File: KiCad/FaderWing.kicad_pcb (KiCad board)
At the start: 2 copper layers, 108 x 240 mm, 242 parts, among them J1 USB_C_Receptacle_USB2.0, SW1 Encoder_Switch, SW10 SW_Push, SW11 Encoder_Switch, SW12 SW_Push, SW13 SW_Push, SW14 SW_Push, SW15 SW_Push, SW16 Encoder_Switch, SW17 SW_Push, SW18 SW_Push, SW19 SW_Push, SW2 SW_Push, SW20 SW_Push, SW21 Encoder_Switch, SW22 SW_Push, SW23 SW_Push, SW24 SW_Push, SW25 SW_Push, SW3 SW_Push, SW4 SW_Push, SW5 SW_Push, SW6 Encoder_Switch, SW7 SW_Push, SW8 SW_Push, SW9 SW_Push, U1 USBLC6-2SC6, U2 STM32G473RCTx, U3 AP2161WG-7, U4 MIC5504-3.3YM5, U5 TXS0102DCU

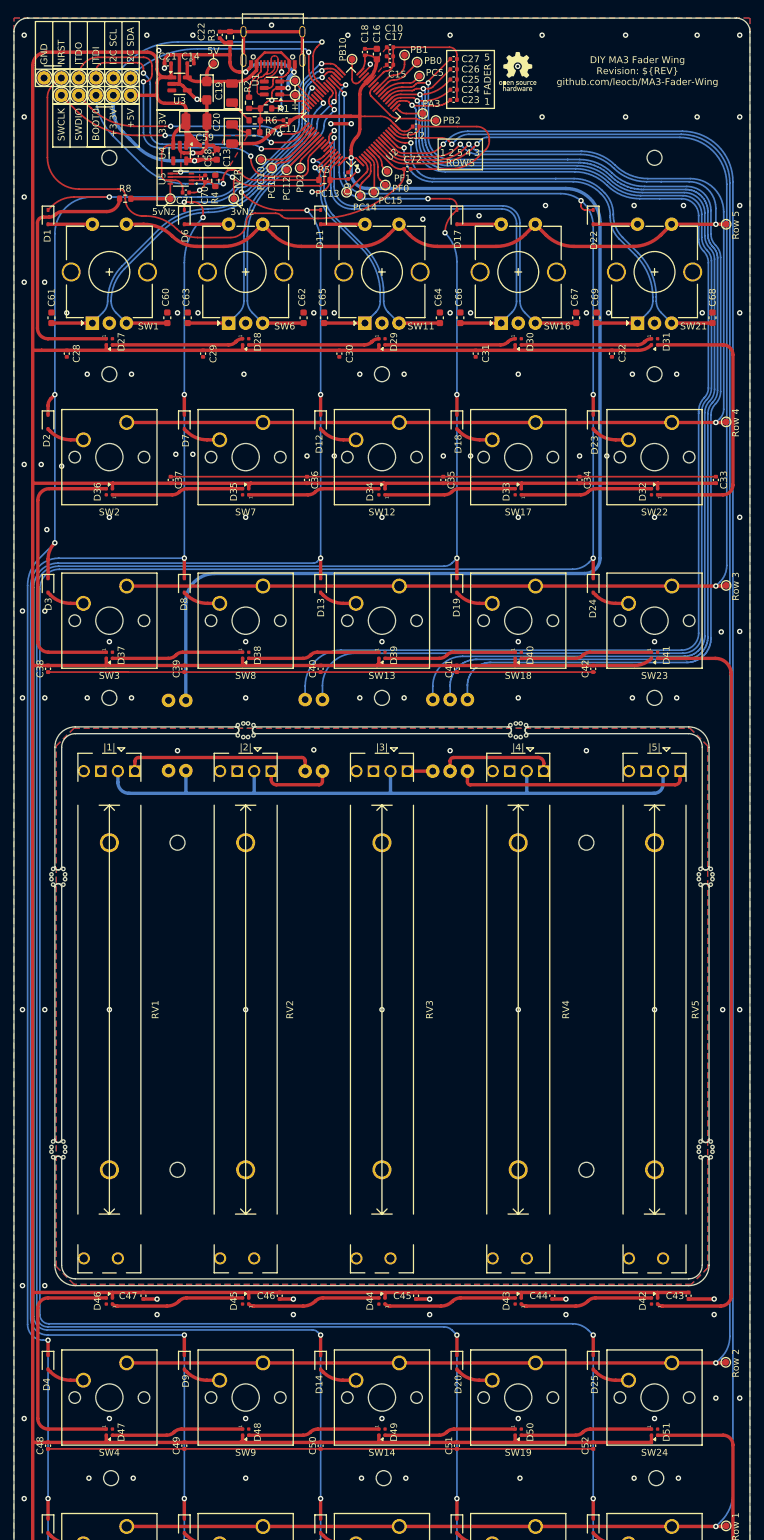
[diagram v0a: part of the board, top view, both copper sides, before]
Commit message: Update components to use less dumb packages
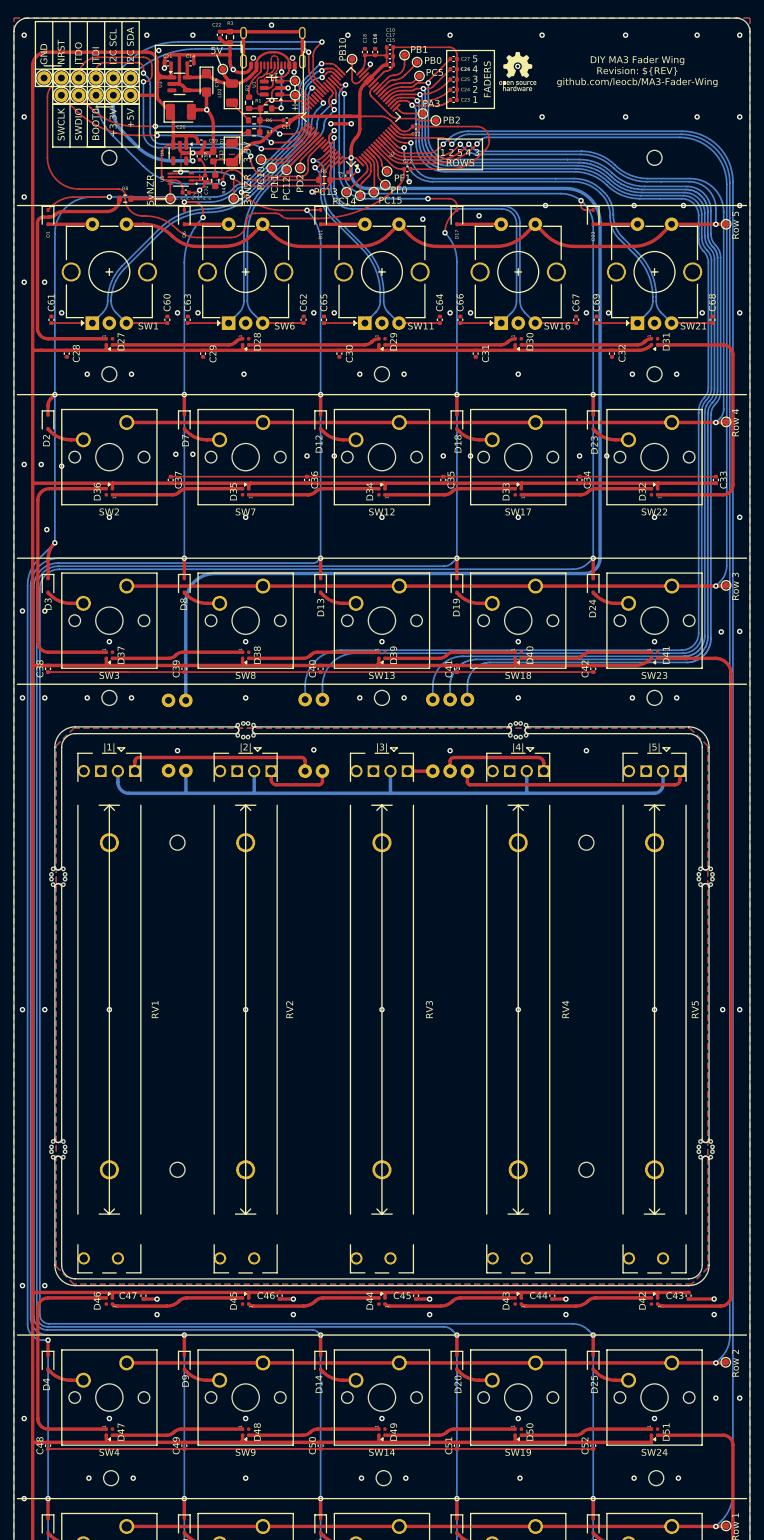
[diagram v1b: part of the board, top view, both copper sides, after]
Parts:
- C16, C60, C61, C62, C63, C64, C65, C66, C67, C68, C69: footprint Capacitor_SMD:C_0603_1608Metric -> Capacitor_SMD:C_0402_1005Metric
- C19: footprint Capacitor_Tantalum_SMD:CP_EIA-3216-10_Kemet-I -> Capacitor_Tantalum_SMD:CP_EIA-3216-18_Kemet-A
- J1: footprint Connector_USB:USB_C_Receptacle_Palconn_UTC16-G -> Connector_USB:USB_C_Receptacle_GCT_USB4105-xx-A_16P_TopMnt_Horizontal
- R3: value 1.02M -> 1M
- R8, R9: value 500 -> 510
- moved LD1 2.75 mm to (53.0, 31.8)
- moved C20 2.68 mm to (45.5, 25.8)
- moved TP29 1.58 mm to (51.6, 19.5)
- moved C19 1.15 mm to (49.2, 21.5)
- moved J1 0.99 mm to (59.0, 15.2)
- moved C13 0.56 mm to (50.2, 32.2)
- moved C59 0.51 mm to (48.5, 30.2)
- moved C16 0.39 mm to (74.0, 17.0)
- moved C60 0.30 mm to (43.5, 56.3)
- moved C61 0.30 mm to (26.5, 56.3)
- moved C62 0.30 mm to (63.5, 56.3)
- moved C63 0.30 mm to (46.5, 56.3)
- moved C64 0.30 mm to (83.5, 56.3)
- moved C65 0.30 mm to (66.5, 56.3)
- moved C66 0.30 mm to (86.5, 56.3)
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- renumbered LED-3V1 to LD1, LED-5V1 to LD2, 3vNz1 to TPNZ1, 5vNz1 to TPNZ2
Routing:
- net +5V: track 890.8 -> 878.5 mm
- net VREF: track 257.8 -> 265.7 mm
- net GND: track 490.0 -> 482.8 mm
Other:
- board text added: "3vNZR"
- board text added: "5vNZR"
- board text added: "<-<-<-<-<-<-<"
- board text added: "FADERS"
- board text removed: "3vNz"
- board text removed: "5vNz"
- board text removed: "FADER"
- board text removed: "NZR"

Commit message: Remove cutout in the middle of the board to reduce costs (custom panelling)
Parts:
- removed TP27, TP28: TestPoint_Small, TestPoint:TestPoint_Pad_D1.0mm
- removed mouse-bite-1mm-slot (x6): VAL**, Custom:mouse-bite-1mm-slot
- R6: value 680 -> 1.2k
- moved U1 2.14 mm to (61.0, 22.2)
- moved R1 1.19 mm to (57.2, 24.3), turned to -90 degrees
- moved R2 0.10 mm to (55.5, 24.3)
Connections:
- B-F1 pad 1: Fader1-sat -> Fader1
- B-F2 pad 1: Fader2-sat -> Fader2
- B-F3 pad 1: Fader3-sat -> Fader3
- B-F4 pad 1: Fader4-sat -> Fader4
- B-F5 pad 1: Fader5-sat -> Fader5
- B-VDDA1 pad 1: Faders-VREF -> VREF
- B-VSSA1 pad 1: Faders-GND -> GND
- RV1 pad 1: Faders-VREF -> VREF
- RV1 pad 2: Fader1-sat -> Fader1
- RV1 pad 3: Faders-GND -> GND
- RV2 pad 1: Faders-VREF -> VREF
- RV2 pad 2: Fader2-sat -> Fader2
- RV2 pad 3: Faders-GND -> GND
- RV3 pad 1: Faders-VREF -> VREF
- RV3 pad 2: Fader3-sat -> Fader3
- RV3 pad 3: Faders-GND -> GND
- RV4 pad 1: Faders-VREF -> VREF
- RV4 pad 2: Fader4-sat -> Fader4
- RV4 pad 3: Faders-GND -> GND
- RV5 pad 1: Faders-VREF -> VREF
- RV5 pad 2: Fader5-sat -> Fader5
- RV5 pad 3: Faders-GND -> GND
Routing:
- net VREF: track 265.7 -> 374.2 mm
- net Faders-VREF: track 98.2 -> 0.00 mm
- net Fader5: track 170.7 -> 215.9 mm
- net Fader1: track 186.2 -> 225.2 mm
- net Fader5-sat: track 34.7 -> 0.00 mm
- net Fader1-sat: track 28.5 -> 0.00 mm
- net Fader4: track 171.3 -> 198.9 mm
- net Fader2: track 185.1 -> 206.5 mm
- net Fader4-sat: track 17.1 -> 0.00 mm
- net Fader3: track 171.0 -> 185.2 mm
- net GND: track 482.8 -> 496.2 mm, vias 145 -> 155
- net Fader2-sat: track 10.9 -> 0.00 mm
- net Fader3-sat: track 3.71 -> 0.00 mm
- net +5VD: track 29.3 -> 27.2 mm
- net USB DP: track 4.84 -> 2.74 mm
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- removed copper zone on B.Cu, net Faders-GND
- removed copper zone on F.Cu, net Faders-GND
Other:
- outline, holes or cut-outs redrawn
- board text removed: "±"
